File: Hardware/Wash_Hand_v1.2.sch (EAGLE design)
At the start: 27 parts, among them J1 I2C, J2 ICSP, J3 SPI, J4 INTERRUPT, J5 EXT_VCC, Q1 16.0 Mhz, U1 328P

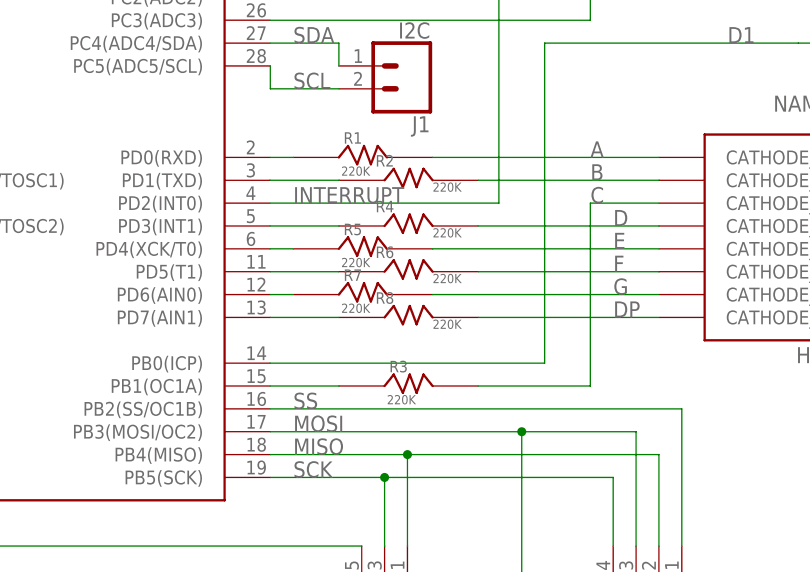
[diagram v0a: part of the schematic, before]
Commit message: Hardware 1.2: Update the registers - it is 220Ohm, not 220K Ohm.
I updated the Wash_Hand_v1.2-routing but forgot the primary one.

Signed-off-by: Konrad Rzeszutek Wilk <konrad@kernel.org>
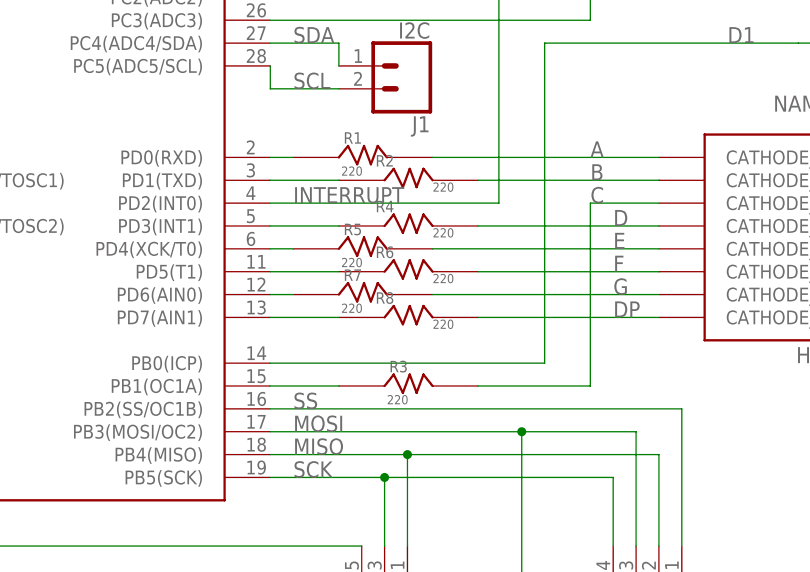
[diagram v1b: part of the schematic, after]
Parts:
- R1, R2, R3, R4, R5, R6, R7, R8: value 220K -> 220
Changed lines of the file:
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@@
 <part name="P+4" library="supply1" library_urn="urn:adsk.eagle:library:371" deviceset="VCC" device=""/>
 <part name="FRAME1" library="frames" library_urn="urn:adsk.eagle:library:229" deviceset="LETTER_L" device=""/>
-<part name="R1" library="PCB_CLASS_PREMADE_COMPONENTS" deviceset="RESISTOR" device="" value="220K"/>
-<part name="R3" library="PCB_CLASS_PREMADE_COMPONENTS" deviceset="RESISTOR" device="" value="220K"/>
-<part name="R5" library="PCB_CLASS_PREMADE_COMPONENTS" deviceset="RESISTOR" device="" value="220K"/>
-<part name="R7" library="PCB_CLASS_PREMADE_COMPONENTS" deviceset="RESISTOR" device="" value="220K"/>
-<part name="R2" library="PCB_CLASS_PREMADE_COMPONENTS" deviceset="RESISTOR" device="" value="220K"/>
-<part name="R4" library="PCB_CLASS_PREMADE_COMPONENTS" deviceset="RESISTOR" device="" value="220K"/>
-<part name="R6" library="PCB_CLASS_PREMADE_COMPONENTS" deviceset="RESISTOR" device="" value="220K"/>
-<part name="R8" library="PCB_CLASS_PREMADE_COMPONENTS" deviceset="RESISTOR" device="" value="220K"/>
+<part name="R1" library="PCB_CLASS_PREMADE_COMPONENTS" deviceset="RESISTOR" device="" value="220"/>
+<part name="R3" library="PCB_CLASS_PREMADE_COMPONENTS" deviceset="RESISTOR" device="" value="220"/>
+<part name="R5" library="PCB_CLASS_PREMADE_COMPONENTS" deviceset="RESISTOR" device="" value="220"/>
+<part name="R7" library="PCB_CLASS_PREMADE_COMPONENTS" deviceset="RESISTOR" device="" value="220"/>
+<part name="R2" library="PCB_CLASS_PREMADE_COMPONENTS" deviceset="RESISTOR" device="" value="220"/>
+<part name="R4" library="PCB_CLASS_PREMADE_COMPONENTS" deviceset="RESISTOR" device="" value="220"/>
+<part name="R6" library="PCB_CLASS_PREMADE_COMPONENTS" deviceset="RESISTOR" device="" value="220"/>
+<part name="R8" library="PCB_CLASS_PREMADE_COMPONENTS" deviceset="RESISTOR" device="" value="220"/>
 <part name="J3" library="SparkFun-Connectors" library_urn="urn:adsk.eagle:library:513" deviceset="CONN_04" device="" package3d_urn="urn:adsk.eagle:package:38085/1" value="SPI"/>
 <part name="H1" library="SparkFun-Hardware" library_urn="urn:adsk.eagle:library:519" deviceset="STAND-OFF" device="" package3d_urn="urn:adsk.eagle:package:38630/1"/>
